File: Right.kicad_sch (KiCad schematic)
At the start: 32 parts, among them J2 Conn_01x02, J4 10103594-0001LF, U2 W25Q128JVS, U3 RP2040, U9 LM1117-3.3, Y1 ECS-120-8-33-JGN-TR3

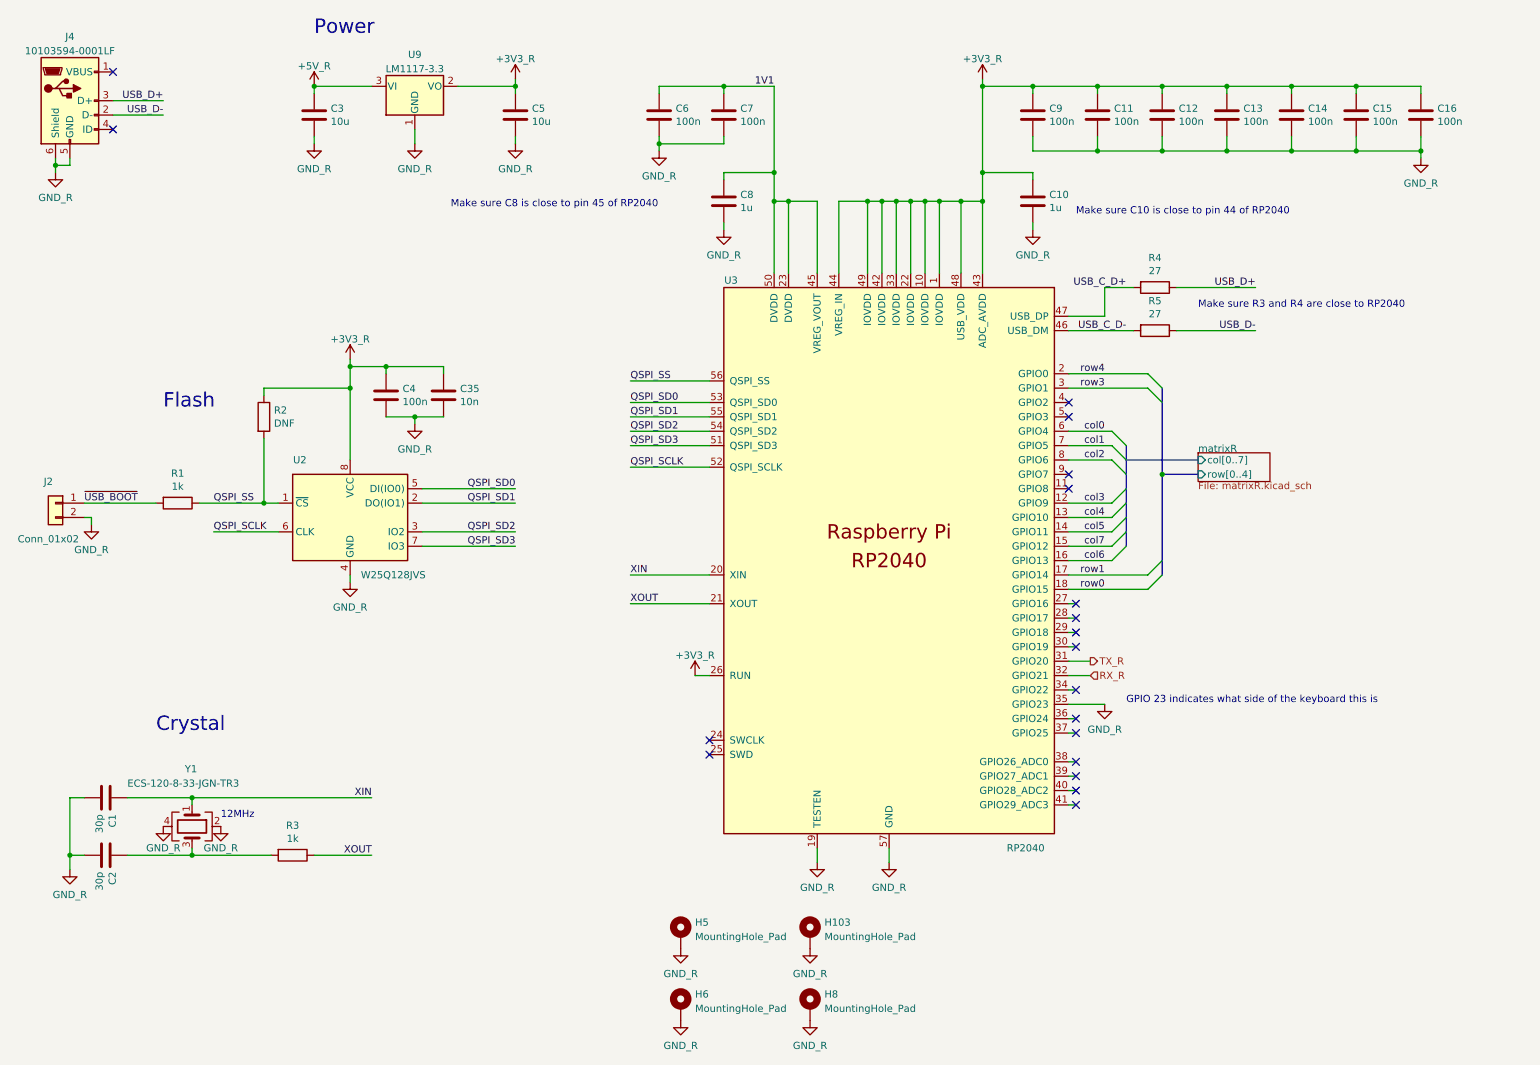
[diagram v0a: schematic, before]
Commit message: replace usb right side, rotate micro, add protection diodes, trrs protection circuit mirrored, run pin cap removved, resistor footprints replaced
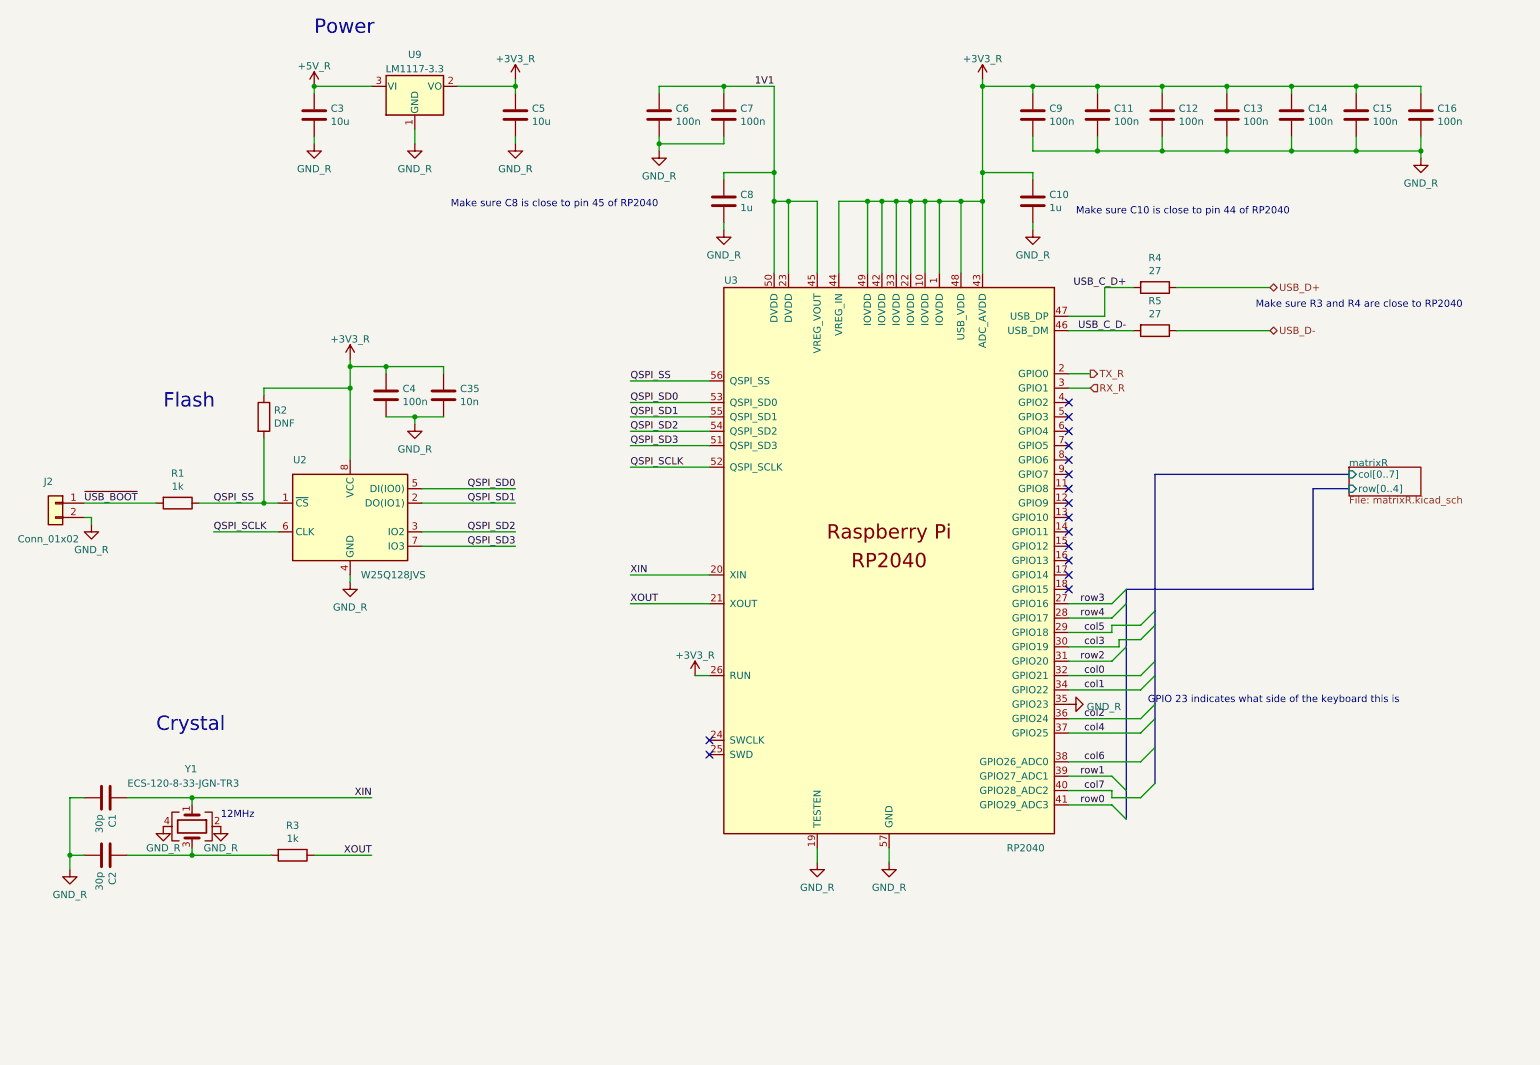
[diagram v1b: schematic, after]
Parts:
- removed H103, H5, H6, H8: MountingHole_Pad, MountingHole:MountingHole_3.2mm_M3_Pad_Via, symbol Mechanical:MountingHole_Pad
- removed J4: 10103594-0001LF, arisu-split:USB_Micro-B_Amphenol_10103594-0001LF_Horizontal, symbol arisu-split:10103594-0001LF
- R1, R2, R4, R5: footprint Capacitor_SMD:C_0603_1608Metric -> Resistor_SMD:R_0603_1608Metric
- R3: footprint Capacitor_SMD:C_0402_1005Metric -> Resistor_SMD:R_0402_1005Metric
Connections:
- net RX_R: now also U3.3 (GPIO1); no longer U3.32 (GPIO21)
- net TX_R: now also U3.2 (GPIO0); no longer U3.31 (GPIO20)
- net col0: now also U3.32 (GPIO21); no longer U3.6 (GPIO4)
- net col1: now also U3.34 (GPIO22); no longer U3.7 (GPIO5)
- net col2: now also U3.36 (GPIO24); no longer U3.8 (GPIO6)
- net col3: now also U3.30 (GPIO19); no longer U3.12 (GPIO9)
- net col4: now also U3.37 (GPIO25); no longer U3.13 (GPIO10)
- net col5: now also U3.29 (GPIO18); no longer U3.14 (GPIO11)
- net col6: now also U3.38 (GPIO26_ADC0); no longer U3.16 (GPIO13)
- net col7: now also U3.40 (GPIO28_ADC2); no longer U3.15 (GPIO12)
- net row0: now also U3.41 (GPIO29_ADC3); no longer U3.18 (GPIO15)
- net row1: now also U3.39 (GPIO27_ADC1); no longer U3.17 (GPIO14)
- net row3: now also U3.27 (GPIO16); no longer U3.3 (GPIO1)
- net row4: now also U3.28 (GPIO17); no longer U3.2 (GPIO0)
- new net row2: U3.31 (GPIO20)
- no-connect marks 19 -> 16

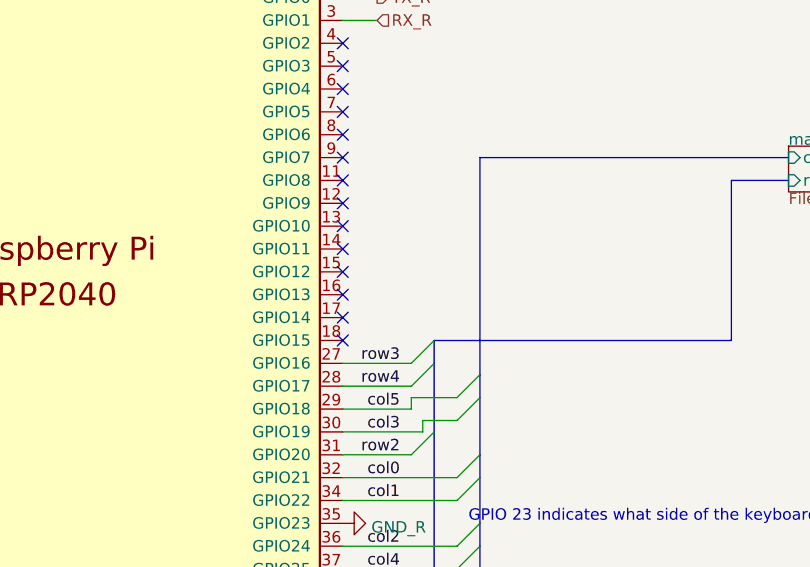
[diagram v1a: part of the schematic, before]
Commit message: Add back logo, improve layers for 3d model, remove silkscreen designators, basically fix right pcb
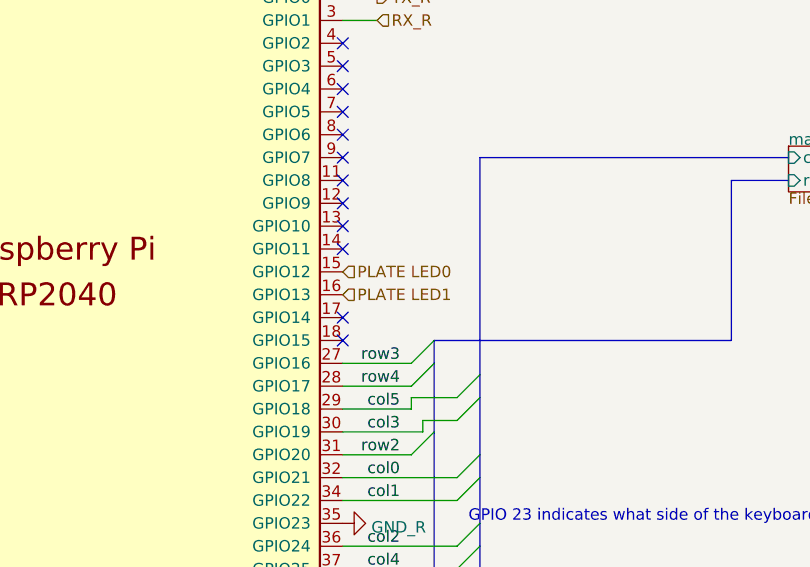
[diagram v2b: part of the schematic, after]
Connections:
- net PLATE LED0: now reaches U3.15 (GPIO12)
- net PLATE LED1: now reaches U3.16 (GPIO13)
- no-connect marks 16 -> 14
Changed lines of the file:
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@@
   (junction (at 172.72 48.26) (diameter 0) (color 0 0 0 0)
   )
-  (no_connect (at 200.66 106.68))
+  (no_connect (at 200.66 88.9))
   (no_connect (at 200.66 116.84))
-  (no_connect (at 200.66 88.9))
   (no_connect (at 200.66 114.3))
   (no_connect (at 200.66 96.52))
@@
   (no_connect (at 200.66 83.82))
   (no_connect (at 137.16 146.05))
-  (no_connect (at 200.66 111.76))
+  (no_connect (at 200.66 106.68))
   (no_connect (at 137.16 143.51))
   (no_connect (at 200.66 101.6))
   (no_connect (at 200.66 93.98))
   (no_connect (at 200.66 86.36))
-  (no_connect (at 200.66 109.22))
   (bus_entry (at 213.36 132.08) (size 2.54 -2.54)
     (stroke (width 0) (type default) (color 0 0 0 0))
@@
     (effects (font (size 1.27 1.27)) (justify left))
   )
+  (hierarchical_label "PLATE LED1" (shape input) (at 200.66 111.76 0)
+    (effects (font (size 1.27 1.27)) (justify left))
+  )
   (hierarchical_label "USB_D+" (shape bidirectional) (at 236.22 63.5 0)
     (effects (font (size 1.27 1.27)) (justify left))
   )
+  (hierarchical_label "PLATE LED0" (shape input) (at 200.66 109.22 0)
+    (effects (font (size 1.27 1.27)) (justify left))
+  )
